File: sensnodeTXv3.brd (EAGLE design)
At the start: 49.4 x 49.6 mm, 36 parts

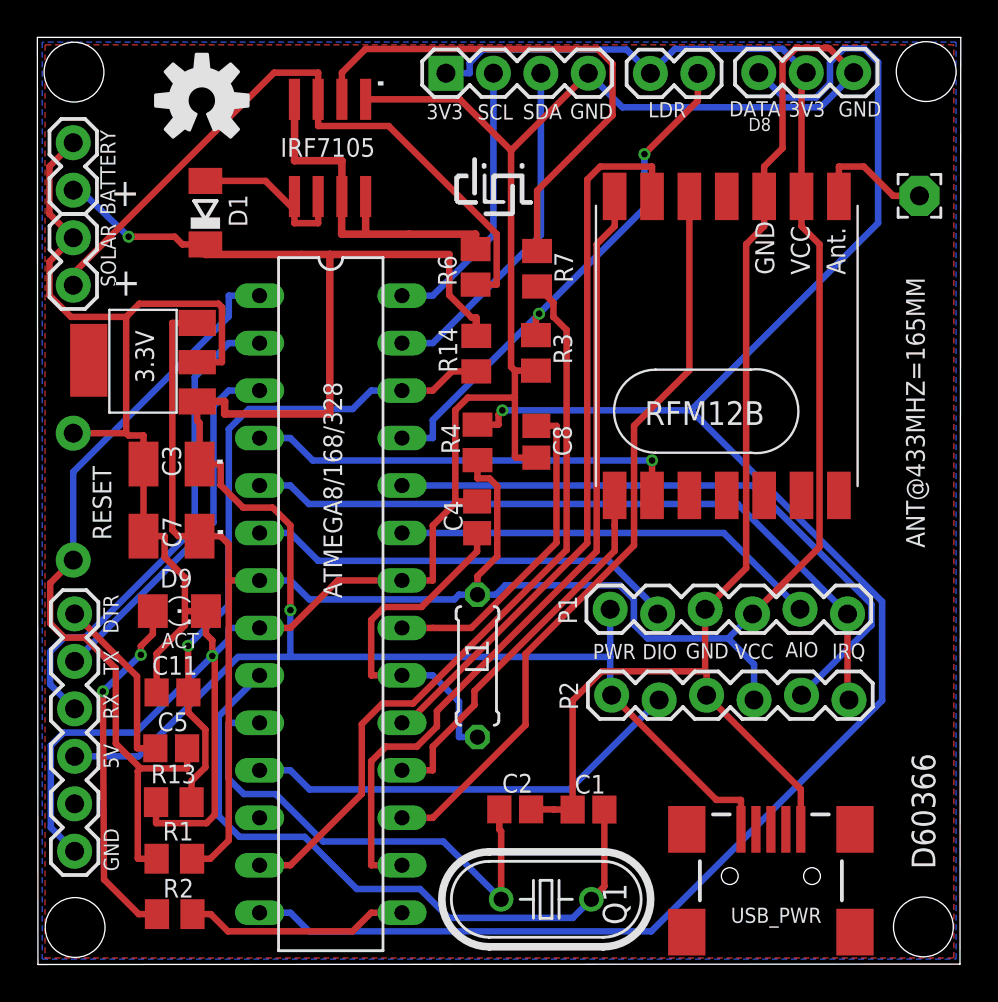
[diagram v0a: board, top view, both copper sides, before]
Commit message: update sensnodeTX and sensbase
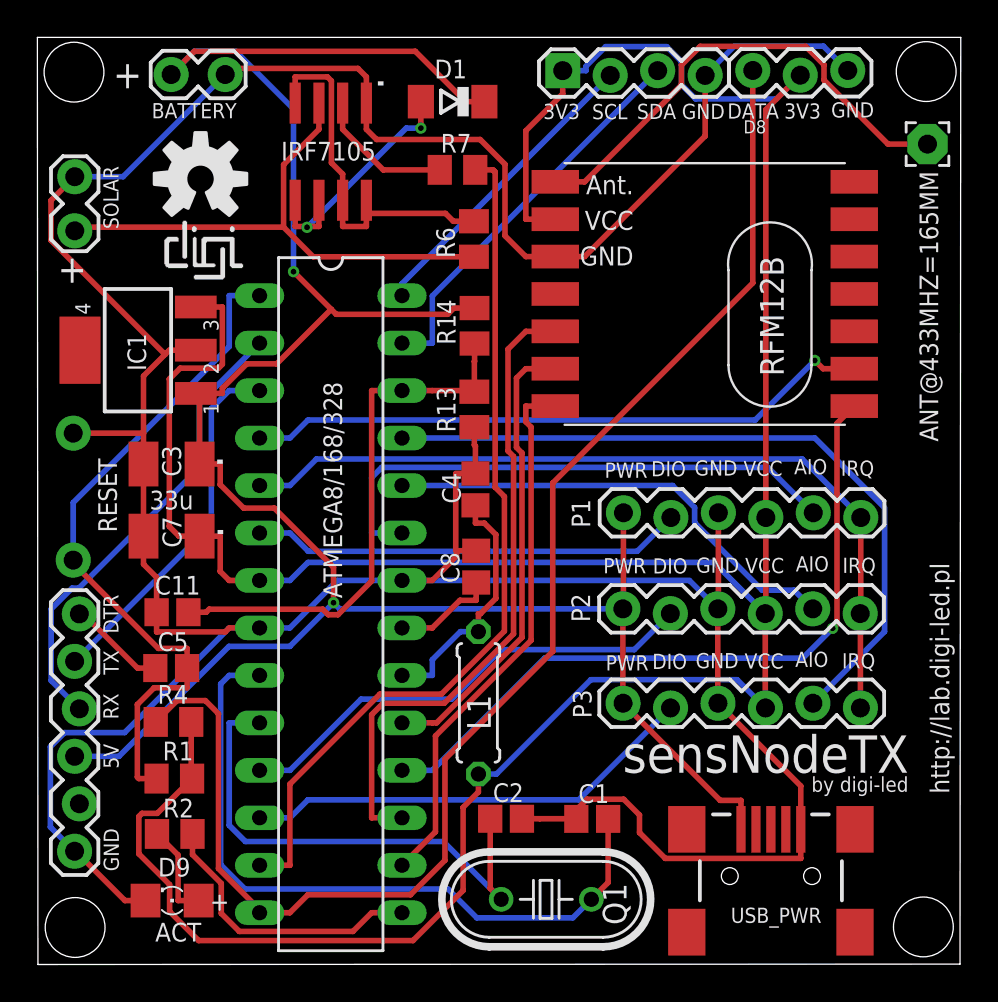
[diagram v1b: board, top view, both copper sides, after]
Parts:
- removed 3.3V: TJ3965-3.3, artek:SOT223
- removed LDR: (no value), SparkFun:1X02
- removed R3: 10k, resistor:M0805
- added IC1: MCP1703DB, linear:SOT223
- added P3: (no value), SparkFun:1X06-SIP_LOCK
- 1-WIRE: device SparkFun:1X03 -> SparkFun:1X03_LOCK
- BATTERY, SOLAR: device SparkFun:1X02 -> SparkFun:1X02_LOCK
- I2C: device SparkFun:1X04 -> SparkFun:1X04_LOCK
- UART: device SparkFun:1X06 -> SparkFun:1X06-SIP_LOCK
- moved R13 26.5 mm to (23.4, 29.7), turned to 90 degrees
- moved R4 22.1 mm to (7.25, 13.0), turned to 0 degrees
- moved ACT 15.5 mm to (7.18, 3.42), turned to 180 degrees
- moved D1 14.5 mm to (22.2, 46.2), turned to 180 degrees
- moved BATTERY 8.22 mm to (7.30, 47.6), turned to 0 degrees
- moved C8 7.42 mm to (23.4, 21.3), turned to 90 degrees
- moved R7 6.79 mm to (22.4, 42.5), turned to 180 degrees
- moved I2C 6.25 mm to (28.1, 47.7)
- moved P1 5.21 mm to (31.3, 24.2)
- moved P2 4.66 mm to (31.3, 19.0)
- moved C11 4.29 mm to (7.20, 18.9)
- moved R2 4.29 mm to (7.32, 6.98)
- moved C5 4.29 mm to (7.13, 15.9)
- moved R1 4.29 mm to (7.30, 9.95)
- moved U$3 4.19 mm to (8.70, 42.0)
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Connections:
- removed net LDR: ATMEGA8/168/328.25, LDR.2, R3.1
- new net N$5: ATMEGA8/168/328.25, P3.5
- new net N$9: ATMEGA8/168/328.12, P3.2
- net +3V3: now also IC1.3, P3.4; no longer 3.3V.OUT, LDR.1
- net DIG3/IRQ: now also P3.6
- net GND: now also IC1.2, P3.3; no longer 3.3V.GND, R3.2
- net VBUS: now also IC1.1, P3.1; no longer 3.3V.IN
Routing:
- net N$5: track 0.00 -> 39.4 mm
- net +3V3: track 130.2 -> 166.7 mm
- net LDR: track 28.3 -> 0.00 mm, vias 2 -> 0
- net 1WIRE: track 102.4 -> 75.9 mm, vias 1 -> 0
- net GND: track 226.3 -> 199.8 mm, vias 1 -> 0
- net N$9: track 0.00 -> 24.4 mm
- net N$12: track 28.4 -> 7.50 mm
- net N$24: track 6.56 -> 26.2 mm
- net DIG12: track 20.4 -> 38.6 mm, vias 0 -> 1
- net VBUS: track 106.9 -> 124.6 mm
- net DIG10: track 43.8 -> 29.1 mm
- net DIG13: track 38.7 -> 24.6 mm
- net N$8: track 19.1 -> 5.14 mm, vias 2 -> 0
- net N$4: track 17.5 -> 5.53 mm
- net DIG2: track 23.4 -> 33.7 mm
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- removed copper zone on layer 1, net N$5
- removed copper zone on layer 16, net N$9
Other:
- board text added: "25/01/2014r"
- board text added: "by digi-led"
- board text added: "http://lab.digi-led.pl"
- board text added: "sensNodeTX"
- board text added: "sensNodeTX v3.5"
- board text removed: "28/09/2012r"
- board text removed: "D60366"
- board text removed: "http://lab.digi-led.pl/sensnode"
- board text removed: "sensNodeTX v3.4"
